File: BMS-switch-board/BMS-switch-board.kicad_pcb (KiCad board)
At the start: 2 copper layers, 20.4 x 61.2 mm, 6 parts, among them J1 Conn_01x08, J2 Conn_01x08, J3 Conn_01x15, J4 Conn_01x15, U1 BQ76200PW, U2 BQ78350DBT-R1

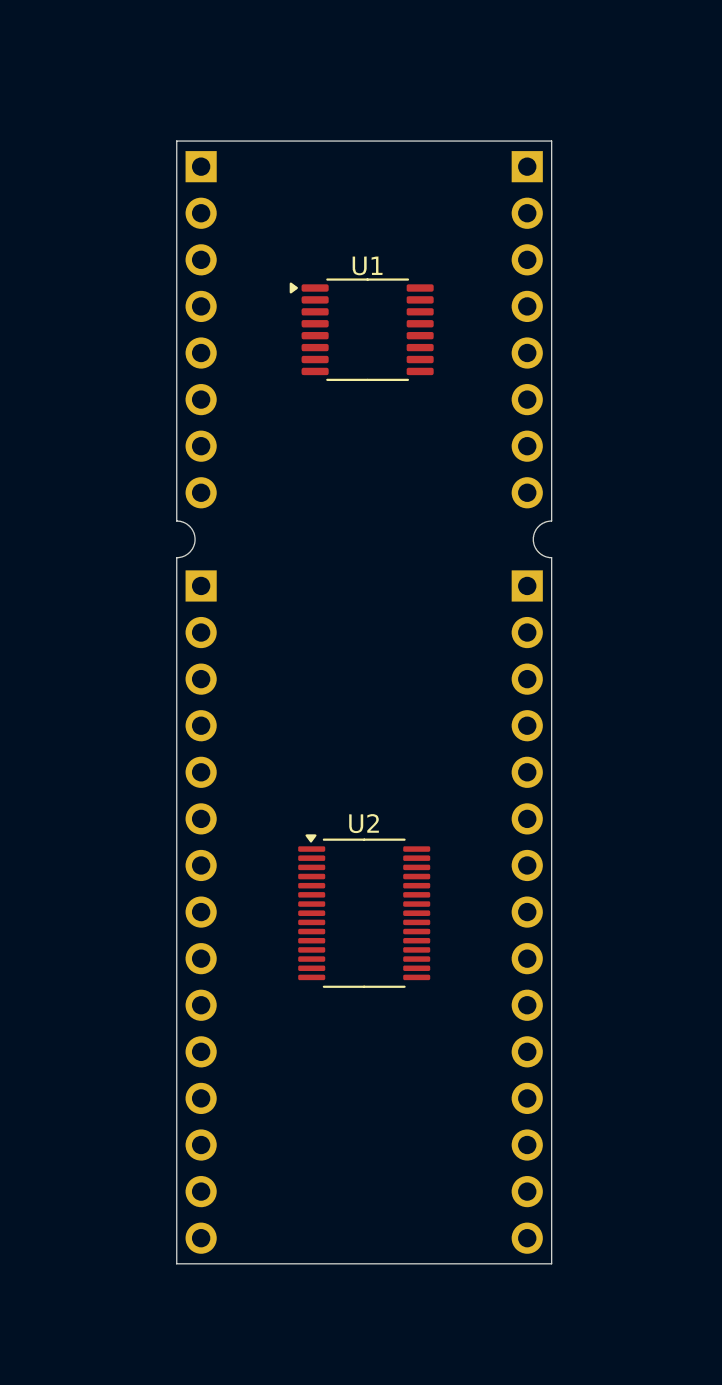
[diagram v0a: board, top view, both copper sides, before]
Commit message: Finished tracks, ground via left
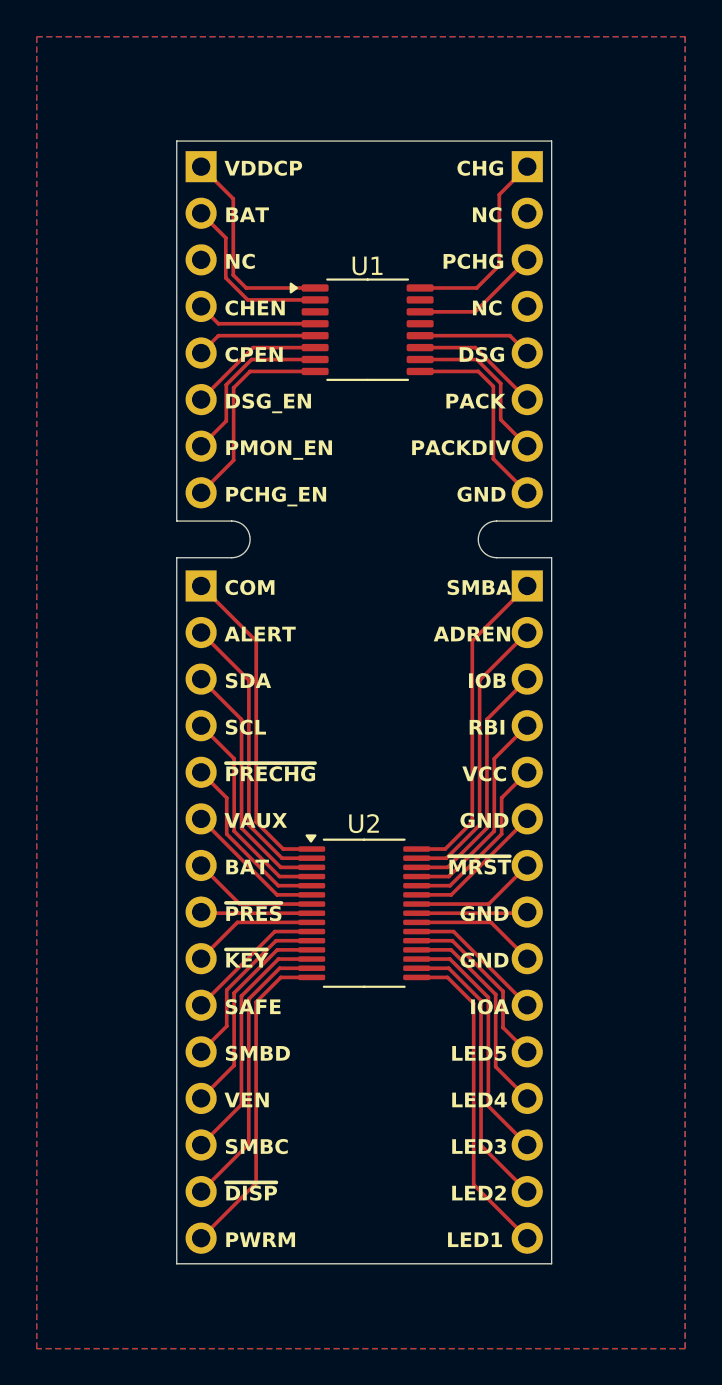
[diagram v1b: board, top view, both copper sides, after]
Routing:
- net GND: track 0.00 -> 31.5 mm
- net /SMBA: track 0.00 -> 17.8 mm
- net /COM: track 0.00 -> 17.8 mm
- net /LED1: track 0.00 -> 17.7 mm
- net /PWRM: track 0.00 -> 17.7 mm
- net /ADREN: track 0.00 -> 15.7 mm
- net /ALERT: track 0.00 -> 15.7 mm
- net /LED2: track 0.00 -> 15.7 mm
- net /~{DISP}: track 0.00 -> 15.7 mm
- net /GPIO_B: track 0.00 -> 13.7 mm
- net /SDA: track 0.00 -> 13.7 mm
- net /LED3: track 0.00 -> 13.7 mm
- net /SMBC: track 0.00 -> 13.7 mm
- net /RBI: track 0.00 -> 11.7 mm
- net /SCL: track 0.00 -> 11.7 mm
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- added copper zone on B.Cu, net GND
- added copper zone on F.Cu, net GND
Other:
- outline, holes or cut-outs redrawn
- board text added: "ADREN"
- board text added: "ALERT"
- board text added: "BAT"
- board text added: "CHEN"
- board text added: "CHG"
- board text added: "COM"
- board text added: "CPEN"
- board text added: "DSG"
- board text added: "DSG_EN"
- board text added: "GND"
- board text added: "IOA"
- board text added: "IOB"
- board text added: "LED1"
- board text added: "LED2"
- board text added: "LED3"
- board text added: "LED4"
- board text added: "LED5"
- board text added: "NC"
- board text added: "PACK"
- board text added: "PACKDIV"
- board text added: "PCHG"
- board text added: "PCHG_EN"
- board text added: "PMON_EN"
- board text added: "PWRM"
- board text added: "RBI"
- board text added: "SAFE"
- board text added: "SCL"
- board text added: "SDA"
- board text added: "SMBA"
- board text added: "SMBC"
- board text added: "SMBD"
- board text added: "VAUX"
- board text added: "VCC"
- board text added: "VDDCP"
- board text added: "VEN"
- board text added: "~{DISP}"
- board text added: "~{KEY}"
- board text added: "~{MRST}"
- board text added: "~{PRECHG}"
- board text added: "~{PRES}"
